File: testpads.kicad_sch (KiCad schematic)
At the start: 47 parts

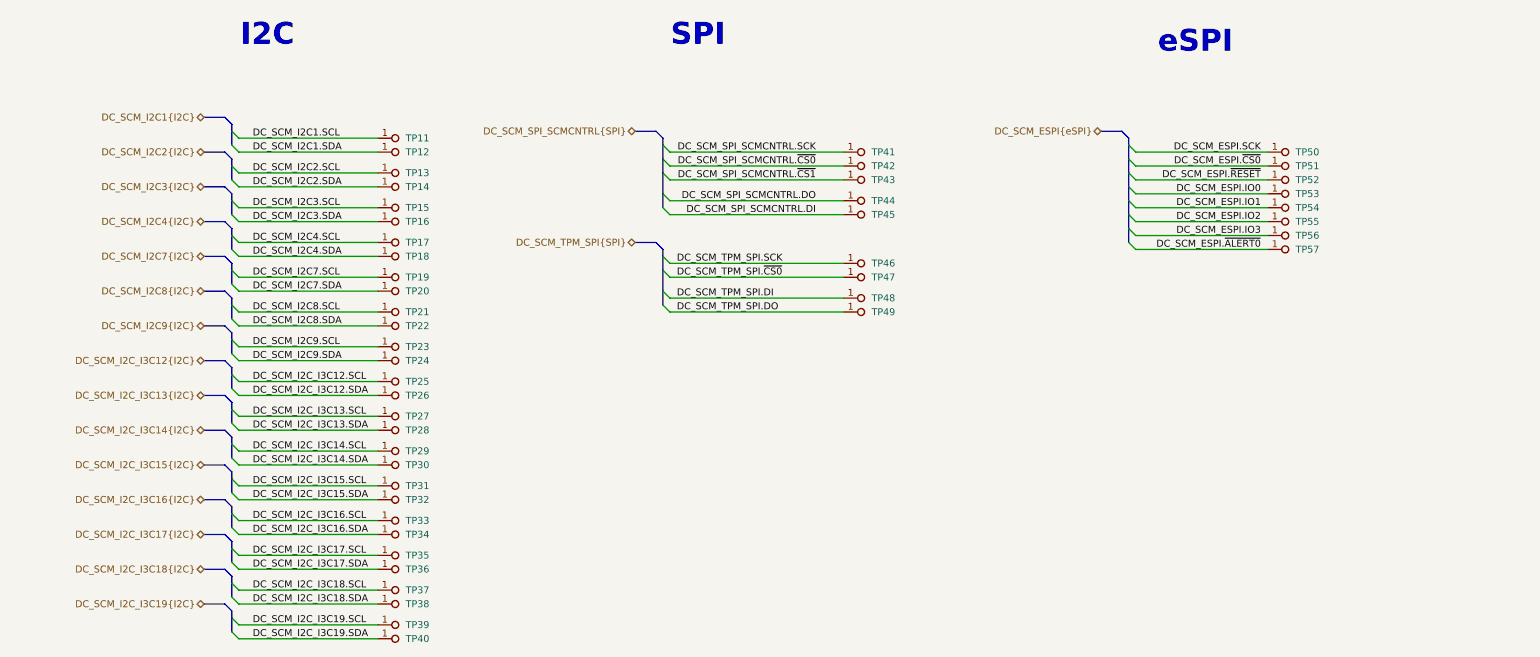
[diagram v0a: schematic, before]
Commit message: [#92504] Change test pads to test pinheaders
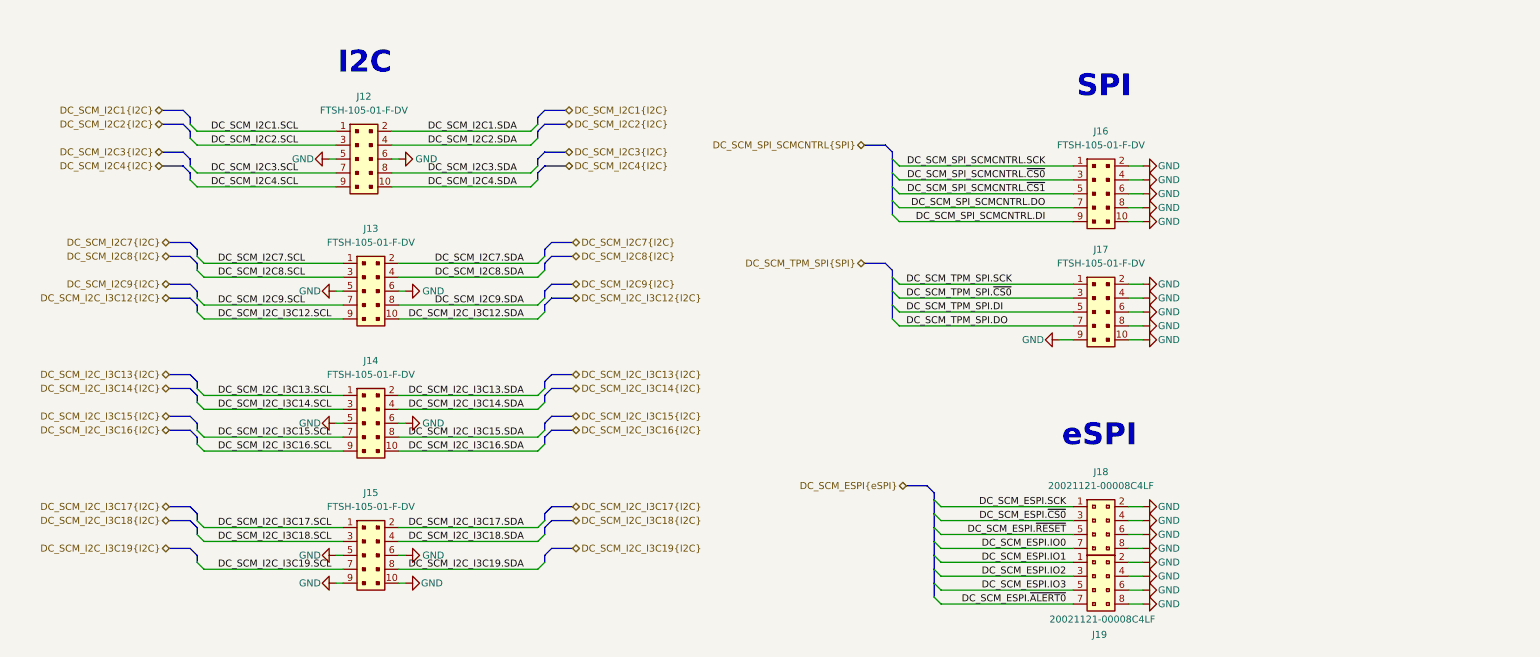
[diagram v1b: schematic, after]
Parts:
- removed TP11, TP12, TP13, TP14, TP15, TP16, TP17, TP18, TP19, TP20, TP21, TP22, TP23, TP24, TP25, TP26, TP27, TP28, TP29, TP30, TP31, TP32, TP33, TP34, TP35, TP36, TP37, TP38, TP39, TP40, TP41, TP42, TP43, TP44, TP45, TP46, TP47, TP48, TP49, TP50, TP51, TP52, TP53, TP54, TP55, TP56, TP57: TP_0.75mm_SMD, antmicro-footprints:TP_SMD_0.75mm, symbol antmicroTestPoints:TP_0.75mm_SMD
- added J12, J13, J14, J15, J16, J17: PinHeader_2x5_P1.27mm_SMD, antmicro-footprints:PinHeader_2x5_P1.27mm_SMD, symbol antmicroGenericPinHeaders:PinHeader_2x5_P1.27mm_SMD
- added J18, J19: PinHeader_2x4_P1.27mm_SMD, antmicro-footprints:PinHeader_2x4_P1.27mm_SMD, symbol antmicroGenericPinHeaders:PinHeader_2x4_P1.27mm_SMD
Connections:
- net DC_SCM_ESPI.IO0: now also J18.7
- net DC_SCM_ESPI.IO1: now also J19.1
- net DC_SCM_ESPI.IO2: now also J19.3
- net DC_SCM_ESPI.IO3: now also J19.5
- net DC_SCM_ESPI.SCK: now also J18.1
- net DC_SCM_ESPI.~{ALERT0}: now also J19.7
- net DC_SCM_ESPI.~{CS0}: now also J18.3
- net DC_SCM_ESPI.~{RESET}: now also J18.5
- net DC_SCM_I2C1.SCL: now also J12.1
- net DC_SCM_I2C1.SDA: now also J12.2
- net DC_SCM_I2C2.SCL: now also J12.3
- net DC_SCM_I2C2.SDA: now also J12.4
- net DC_SCM_I2C3.SCL: now also J12.7
- net DC_SCM_I2C3.SDA: now also J12.8
- net DC_SCM_I2C4.SCL: now also J12.9
- net DC_SCM_I2C4.SDA: now also J12.10
- net DC_SCM_I2C7.SCL: now also J13.1
- net DC_SCM_I2C7.SDA: now also J13.2
- net DC_SCM_I2C8.SCL: now also J13.3
- net DC_SCM_I2C8.SDA: now also J13.4
- net DC_SCM_I2C9.SCL: now also J13.7
- net DC_SCM_I2C9.SDA: now also J13.8
- net DC_SCM_I2C_I3C12.SCL: now also J13.9
- net DC_SCM_I2C_I3C12.SDA: now also J13.10
- net DC_SCM_I2C_I3C13.SCL: now also J14.1
- net DC_SCM_I2C_I3C13.SDA: now also J14.2
- net DC_SCM_I2C_I3C14.SCL: now also J14.3
- net DC_SCM_I2C_I3C14.SDA: now also J14.4
- net DC_SCM_I2C_I3C15.SCL: now also J14.7
- net DC_SCM_I2C_I3C15.SDA: now also J14.8
- net DC_SCM_I2C_I3C16.SCL: now also J14.9
- net DC_SCM_I2C_I3C16.SDA: now also J14.10
- net DC_SCM_I2C_I3C17.SCL: now also J15.1
- net DC_SCM_I2C_I3C17.SDA: now also J15.2
- net DC_SCM_I2C_I3C18.SCL: now also J15.3
- net DC_SCM_I2C_I3C18.SDA: now also J15.4
- net DC_SCM_I2C_I3C19.SCL: now also J15.7
- net DC_SCM_I2C_I3C19.SDA: now also J15.8
- net DC_SCM_SPI_SCMCNTRL.DI: now also J16.9
- net DC_SCM_SPI_SCMCNTRL.DO: now also J16.7
- net DC_SCM_SPI_SCMCNTRL.SCK: now also J16.1
- net DC_SCM_SPI_SCMCNTRL.~{CS0}: now also J16.3
- net DC_SCM_SPI_SCMCNTRL.~{CS1}: now also J16.5
- net DC_SCM_TPM_SPI.DI: now also J17.5
- net DC_SCM_TPM_SPI.DO: now also J17.7
- net DC_SCM_TPM_SPI.SCK: now also J17.1
- net DC_SCM_TPM_SPI.~{CS0}: now also J17.3
- new net GND: J12.5, J12.6, J13.5, J13.6, J14.5, J14.6, J15.10, J15.5, J15.6, J15.9, J16.10, J16.2, J16.4, J16.6, J16.8, J17.10, J17.2, J17.4, J17.6, J17.8, J17.9, J18.2, J18.4, J18.6, J18.8, J19.2, J19.4, J19.6, J19.8

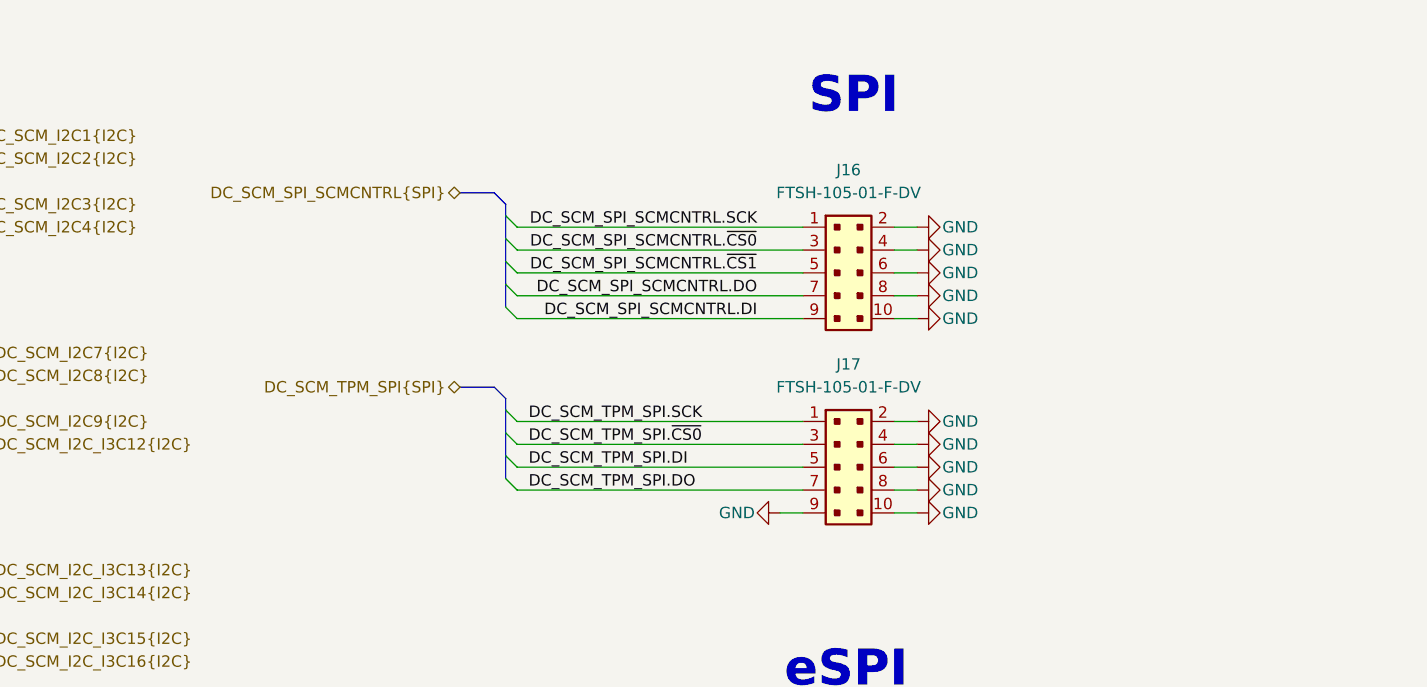
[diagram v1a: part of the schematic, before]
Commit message: [#92504] Flip SPI pins
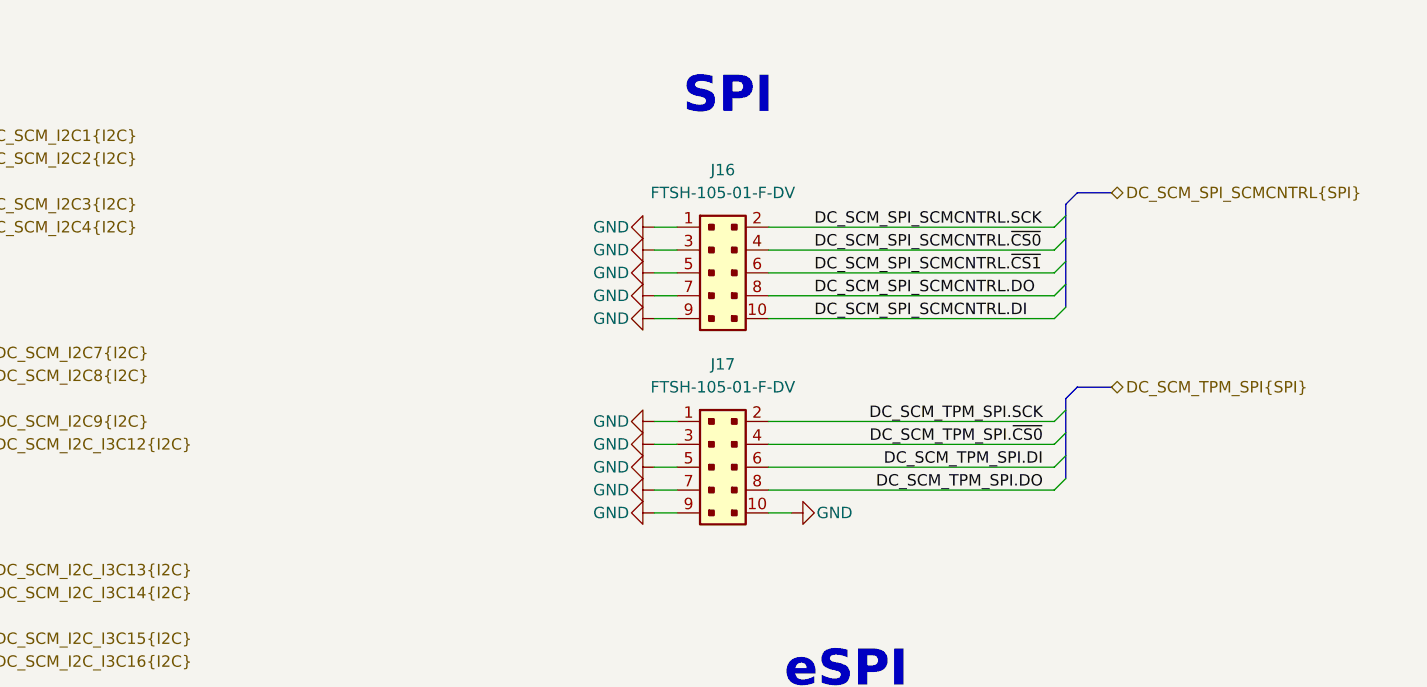
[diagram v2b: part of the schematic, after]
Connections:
- net DC_SCM_SPI_SCMCNTRL.DI: now also J16.10; no longer J16.9
- net DC_SCM_SPI_SCMCNTRL.DO: now also J16.8; no longer J16.7
- net DC_SCM_SPI_SCMCNTRL.SCK: now also J16.2; no longer J16.1
- net DC_SCM_SPI_SCMCNTRL.~{CS0}: now also J16.4; no longer J16.3
- net DC_SCM_SPI_SCMCNTRL.~{CS1}: now also J16.6; no longer J16.5
- net DC_SCM_TPM_SPI.DI: now also J17.6; no longer J17.5
- net DC_SCM_TPM_SPI.DO: now also J17.8; no longer J17.7
- net DC_SCM_TPM_SPI.SCK: now also J17.2; no longer J17.1
- net DC_SCM_TPM_SPI.~{CS0}: now also J17.4; no longer J17.3
- net GND: now also J16.1, J16.3, J16.5, J16.7, J16.9, J17.1, J17.3, J17.5, J17.7; no longer J16.10, J16.2, J16.4, J16.6, J16.8, J17.2, J17.4, J17.6, J17.8
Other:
- moved on the sheet: J16, J17

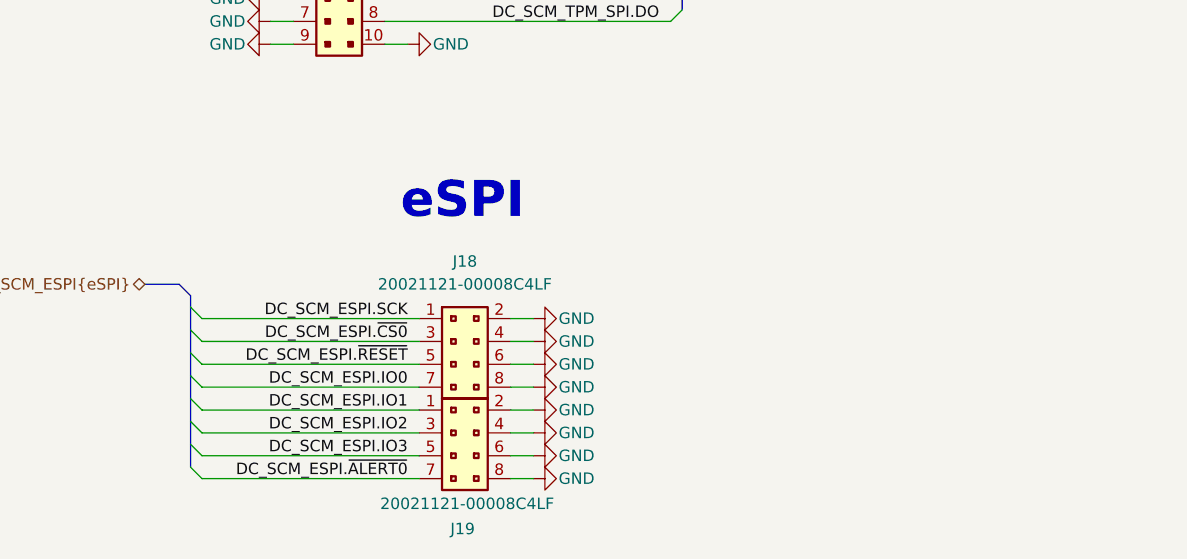
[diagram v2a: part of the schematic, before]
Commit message: [#92504] Change eSPI connector to 2x05
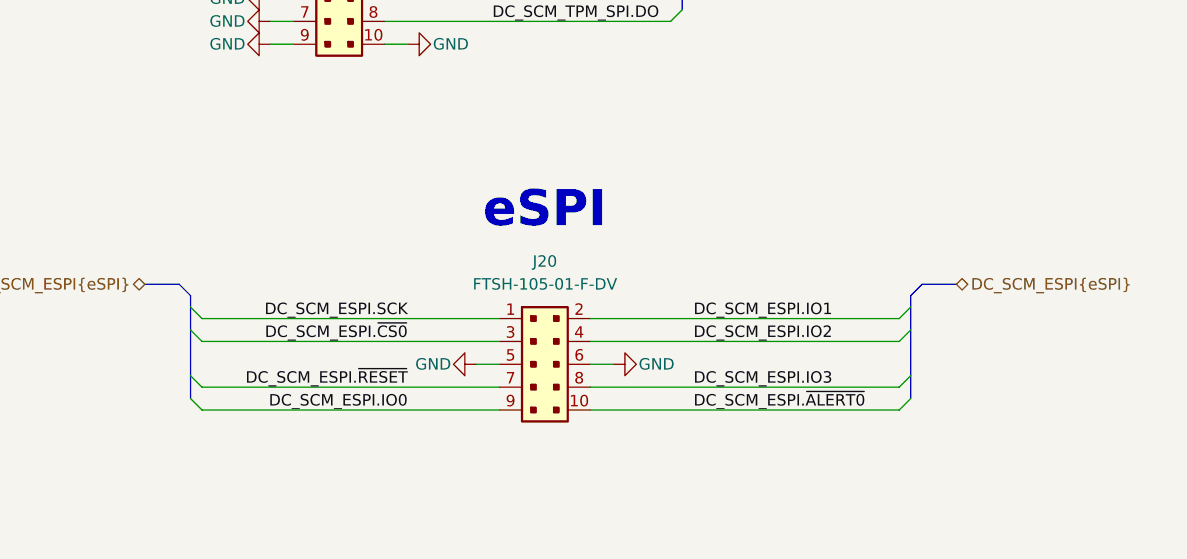
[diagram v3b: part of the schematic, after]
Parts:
- removed J18, J19: PinHeader_2x4_P1.27mm_SMD, antmicro-footprints:PinHeader_2x4_P1.27mm_SMD, symbol antmicroGenericPinHeaders:PinHeader_2x4_P1.27mm_SMD
- added J20: PinHeader_2x5_P1.27mm_SMD, antmicro-footprints:PinHeader_2x5_P1.27mm_SMD, symbol antmicroGenericPinHeaders:PinHeader_2x5_P1.27mm_SMD
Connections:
- net DC_SCM_ESPI.IO0: now also J20.9
- net DC_SCM_ESPI.IO1: now also J20.2
- net DC_SCM_ESPI.IO2: now also J20.4
- net DC_SCM_ESPI.IO3: now also J20.8
- net DC_SCM_ESPI.SCK: now also J20.1
- net DC_SCM_ESPI.~{ALERT0}: now also J20.10
- net DC_SCM_ESPI.~{CS0}: now also J20.3
- net DC_SCM_ESPI.~{RESET}: now also J20.7
- net GND: now also J20.5, J20.6
